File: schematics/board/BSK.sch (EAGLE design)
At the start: 56 parts

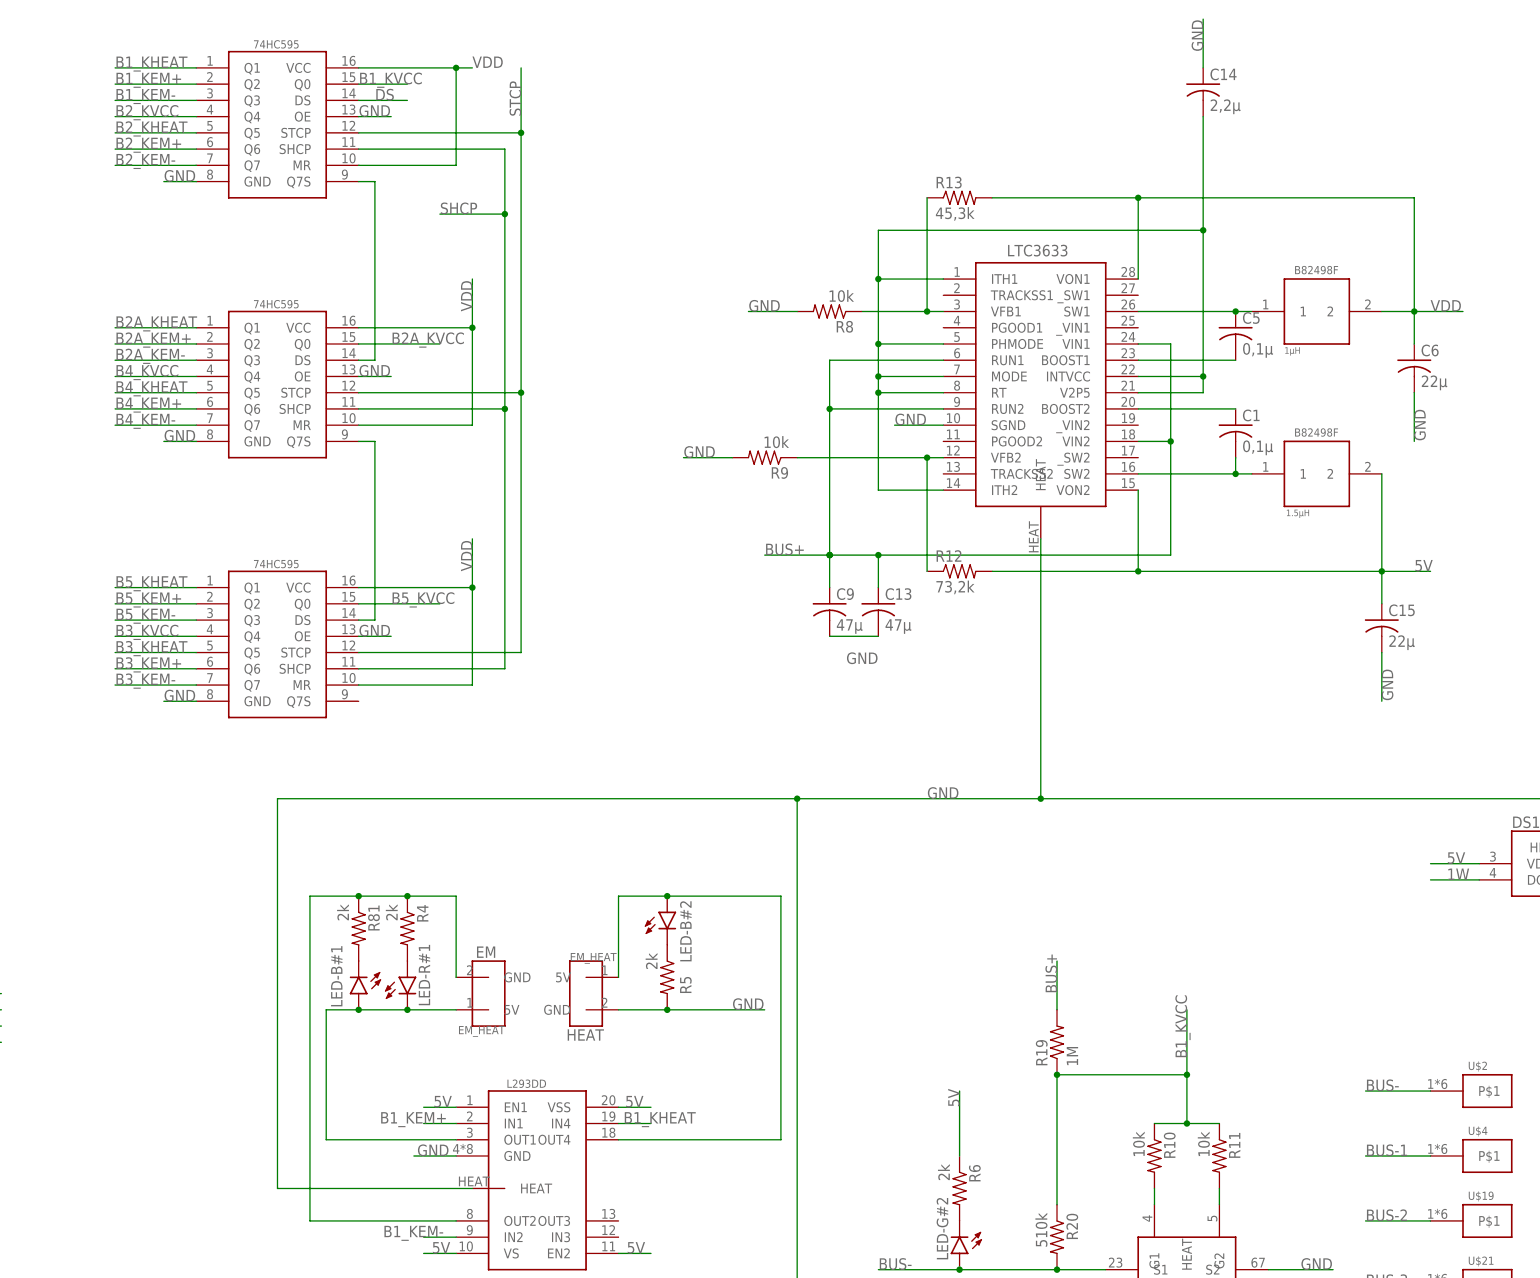
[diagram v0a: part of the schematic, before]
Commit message: Плата АРК проложена на 76%
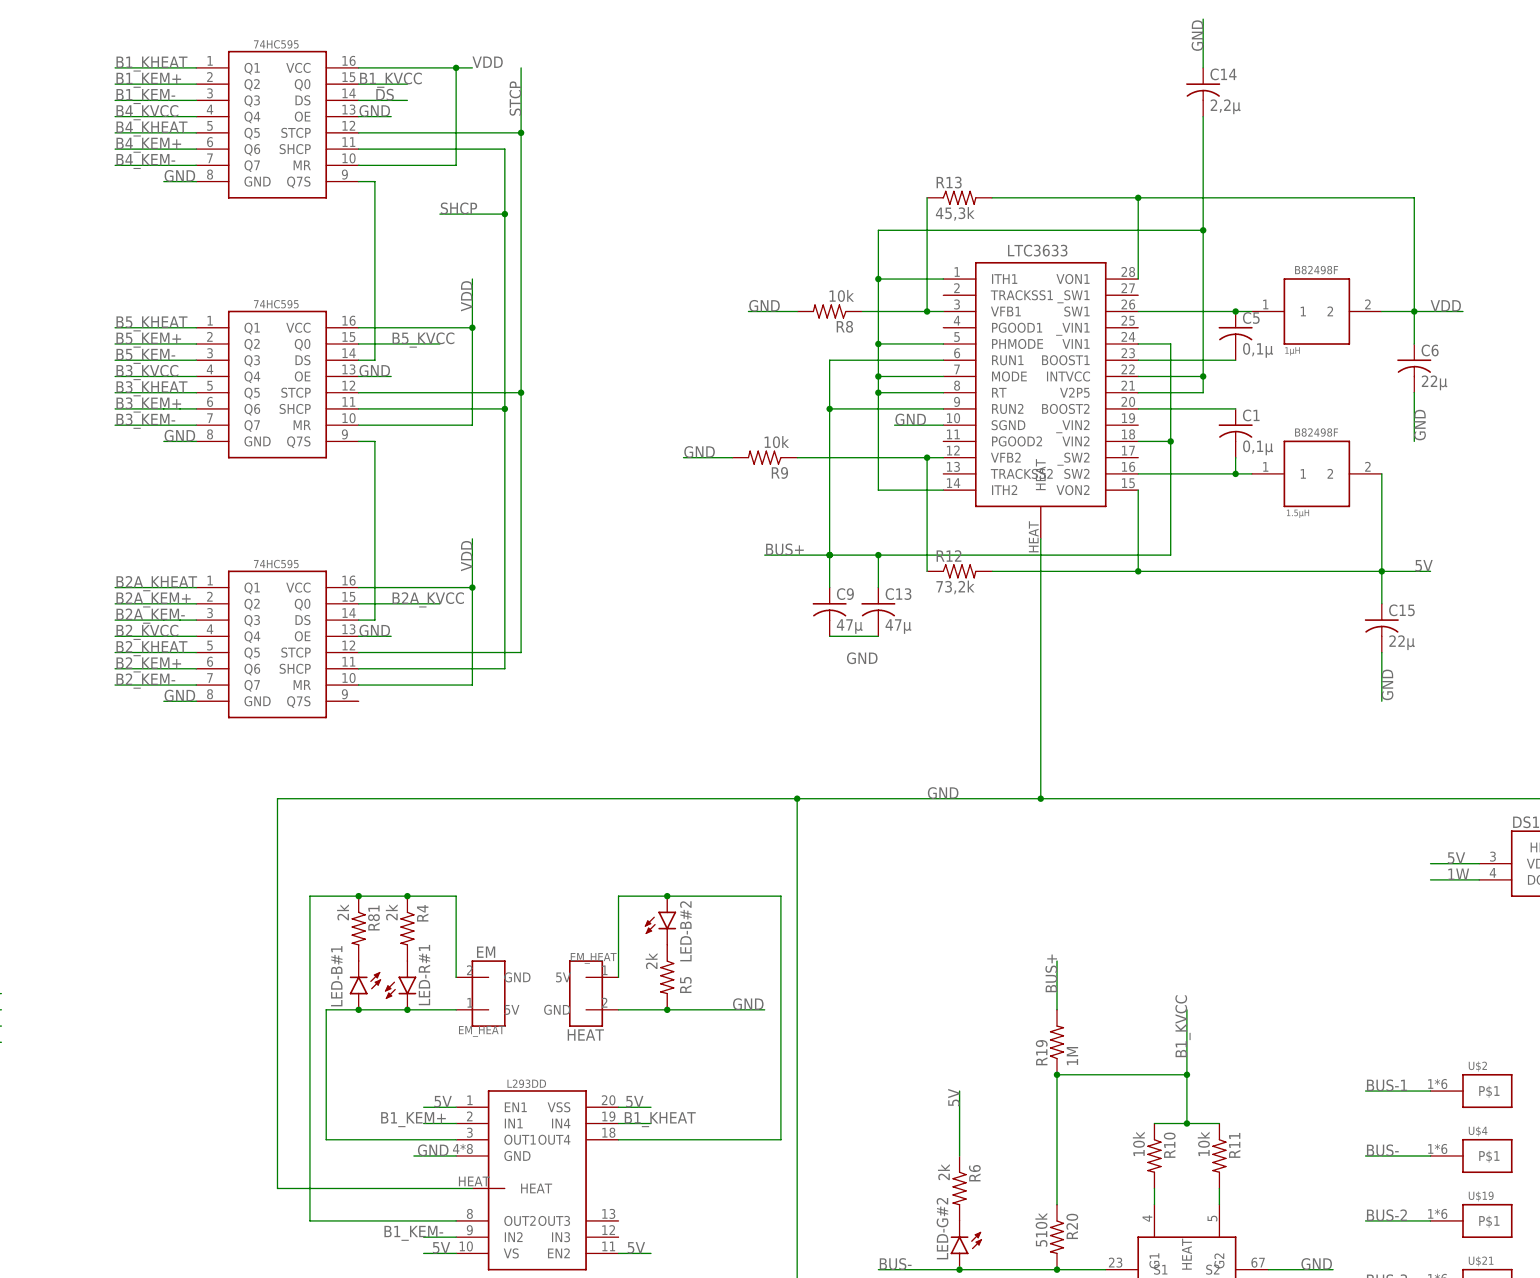
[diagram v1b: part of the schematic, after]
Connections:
- net B2A_KEM+: now also 74HC595#3.Q2; no longer 74HC595#2.Q2
- net B2A_KEM-: now also 74HC595#3.Q3; no longer 74HC595#2.Q3
- net B2A_KHEAT: now also 74HC595#3.Q1; no longer 74HC595#2.Q1
- net B2A_KVCC: now also 74HC595#3.Q0; no longer 74HC595#2.Q0
- net B2_KEM+: now also 74HC595#3.Q6; no longer 74HC595#1.Q6
- net B2_KEM-: now also 74HC595#3.Q7; no longer 74HC595#1.Q7
- net B2_KHEAT: now also 74HC595#3.Q5; no longer 74HC595#1.Q5
- net B2_KVCC: now also 74HC595#3.Q4; no longer 74HC595#1.Q4
- net B3_KEM+: now also 74HC595#2.Q6; no longer 74HC595#3.Q6
- net B3_KEM-: now also 74HC595#2.Q7; no longer 74HC595#3.Q7
- net B3_KHEAT: now also 74HC595#2.Q5; no longer 74HC595#3.Q5
- net B3_KVCC: now also 74HC595#2.Q4; no longer 74HC595#3.Q4
- net B4_KEM+: now also 74HC595#1.Q6; no longer 74HC595#2.Q6
- net B4_KEM-: now also 74HC595#1.Q7; no longer 74HC595#2.Q7
- net B4_KHEAT: now also 74HC595#1.Q5; no longer 74HC595#2.Q5
- net B4_KVCC: now also 74HC595#1.Q4; no longer 74HC595#2.Q4
- net B5_KEM+: now also 74HC595#2.Q2; no longer 74HC595#3.Q2
- net B5_KEM-: now also 74HC595#2.Q3; no longer 74HC595#3.Q3
- net B5_KHEAT: now also 74HC595#2.Q1; no longer 74HC595#3.Q1
- net B5_KVCC: now also 74HC595#2.Q0; no longer 74HC595#3.Q0
- net BUS-: now also U$4.P$1; no longer U$2.P$1
- net BUS-1: now also U$2.P$1; no longer U$4.P$1
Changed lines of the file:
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@@
 <net name="B2_KEM+" class="0">
 <segment>
-<pinref part="74HC595#1" gate="G$1" pin="Q6"/>
-<wire x1="104.14" y1="264.16" x2="91.44" y2="264.16" width="0.1524" layer="91"/>
-<label x="91.44" y="264.16" size="1.778" layer="95"/>
+<label x="91.44" y="182.88" size="1.778" layer="95"/>
+<wire x1="104.14" y1="182.88" x2="91.44" y2="182.88" width="0.1524" layer="91"/>
+<pinref part="74HC595#3" gate="G$1" pin="Q6"/>
 </segment>
 <segment>
@@
 <net name="B2_KEM-" class="0">
 <segment>
-<pinref part="74HC595#1" gate="G$1" pin="Q7"/>
-<wire x1="104.14" y1="261.62" x2="91.44" y2="261.62" width="0.1524" layer="91"/>
-<label x="91.44" y="261.62" size="1.778" layer="95"/>
+<label x="91.44" y="180.34" size="1.778" layer="95"/>
+<wire x1="104.14" y1="180.34" x2="91.44" y2="180.34" width="0.1524" layer="91"/>
+<pinref part="74HC595#3" gate="G$1" pin="Q7"/>
 </segment>
 <segment>
@@
 <net name="B2_KHEAT" class="0">
 <segment>
-<pinref part="74HC595#1" gate="G$1" pin="Q5"/>
-<wire x1="104.14" y1="266.7" x2="91.44" y2="266.7" width="0.1524" layer="91"/>
-<label x="91.44" y="266.7" size="1.778" layer="95"/>
+<label x="91.44" y="185.42" size="1.778" layer="95"/>
+<wire x1="104.14" y1="185.42" x2="91.44" y2="185.42" width="0.1524" layer="91"/>
+<pinref part="74HC595#3" gate="G$1" pin="Q5"/>
 </segment>
 <segment>
@@
 <net name="B2A_KEM+" class="0">
 <segment>
-<pinref part="74HC595#2" gate="G$1" pin="Q2"/>
-<wire x1="104.14" y1="233.68" x2="91.44" y2="233.68" width="0.1524" layer="91"/>
-<label x="91.44" y="233.68" size="1.778" layer="95"/>
+<label x="91.44" y="193.04" size="1.778" layer="95"/>
+<wire x1="104.14" y1="193.04" x2="91.44" y2="193.04" width="0.1524" layer="91"/>
+<pinref part="74HC595#3" gate="G$1" pin="Q2"/>
 </segment>
 <segment>
@@
 <net name="B2A_KEM-" class="0">
 <segment>
-<pinref part="74HC595#2" gate="G$1" pin="Q3"/>
-<wire x1="104.14" y1="231.14" x2="91.44" y2="231.14" width="0.1524" layer="91"/>
-<label x="91.44" y="231.14" size="1.778" layer="95"/>
+<label x="91.44" y="190.5" size="1.778" layer="95"/>
+<wire x1="101.6" y1="190.5" x2="99.06" y2="190.5" width="0.1524" layer="91"/>
+<pinref part="74HC595#3" gate="G$1" pin="Q3"/>
+<wire x1="99.06" y1="190.5" x2="91.44" y2="190.5" width="0.1524" layer="91"/>
+<wire x1="101.6" y1="190.5" x2="104.14" y2="190.5" width="0.1524" layer="91"/>
 </segment>
 <segment>
@@
 <net name="B2A_KHEAT" class="0">
 <segment>
-<pinref part="74HC595#2" gate="G$1" pin="Q1"/>
-<wire x1="104.14" y1="236.22" x2="91.44" y2="236.22" width="0.1524" layer="91"/>
-<label x="91.44" y="236.22" size="1.778" layer="95"/>
+<label x="91.44" y="195.58" size="1.778" layer="95"/>
+<wire x1="104.14" y1="195.58" x2="91.44" y2="195.58" width="0.1524" layer="91"/>
+<pinref part="74HC595#3" gate="G$1" pin="Q1"/>
 </segment>
 <segment>
@@
 </segment>
 <segment>
-<pinref part="74HC595#3" gate="G$1" pin="Q6"/>
-<wire x1="104.14" y1="182.88" x2="91.44" y2="182.88" width="0.1524" layer="91"/>
-<label x="91.44" y="182.88" size="1.778" layer="95"/>
+<label x="91.44" y="223.52" size="1.778" layer="95"/>
+<wire x1="101.6" y1="223.52" x2="99.06" y2="223.52" width="0.1524" layer="91"/>
+<pinref part="74HC595#2" gate="G$1" pin="Q6"/>
+<wire x1="99.06" y1="223.52" x2="91.44" y2="223.52" width="0.1524" layer="91"/>
+<wire x1="104.14" y1="223.52" x2="101.6" y2="223.52" width="0.1524" layer="91"/>
 </segment>
 </net>
@@
 </segment>
 <segment>
-<pinref part="74HC595#3" gate="G$1" pin="Q7"/>
-<wire x1="104.14" y1="180.34" x2="91.44" y2="180.34" width="0.1524" layer="91"/>
-<label x="91.44" y="180.34" size="1.778" layer="95"/>
+<label x="91.44" y="220.98" size="1.778" layer="95"/>
+<wire x1="104.14" y1="220.98" x2="91.44" y2="220.98" width="0.1524" layer="91"/>
+<pinref part="74HC595#2" gate="G$1" pin="Q7"/>
 </segment>
 </net>
@@
 </segment>
 <segment>
-<pinref part="74HC595#3" gate="G$1" pin="Q5"/>
-<wire x1="104.14" y1="185.42" x2="91.44" y2="185.42" width="0.1524" layer="91"/>
-<label x="91.44" y="185.42" size="1.778" layer="95"/>
+<label x="91.44" y="226.06" size="1.778" layer="95"/>
+<wire x1="104.14" y1="226.06" x2="91.44" y2="226.06" width="0.1524" layer="91"/>
+<pinref part="74HC595#2" gate="G$1" pin="Q5"/>
 </segment>
 </net>
@@
 </segment>
 <segment>
-<pinref part="74HC595#2" gate="G$1" pin="Q5"/>
-<wire x1="104.14" y1="226.06" x2="91.44" y2="226.06" width="0.1524" layer="91"/>
-<label x="91.44" y="226.06" size="1.778" layer="95"/>
+<label x="91.44" y="266.7" size="1.778" layer="95"/>
+<wire x1="104.14" y1="266.7" x2="91.44" y2="266.7" width="0.1524" layer="91"/>
+<pinref part="74HC595#1" gate="G$1" pin="Q5"/>
 </segment>
 </net>
 <net name="B5_KEM+" class="0">
 <segment>
-<pinref part="74HC595#3" gate="G$1" pin="Q2"/>
-<wire x1="104.14" y1="193.04" x2="91.44" y2="193.04" width="0.1524" layer="91"/>
-<label x="91.44" y="193.04" size="1.778" layer="95"/>
+<label x="91.44" y="233.68" size="1.778" layer="95"/>
+<wire x1="104.14" y1="233.68" x2="91.44" y2="233.68" width="0.1524" layer="91"/>
+<pinref part="74HC595#2" gate="G$1" pin="Q2"/>
 </segment>
 <segment>
@@
 <net name="B5_KEM-" class="0">
 <segment>
-<pinref part="74HC595#3" gate="G$1" pin="Q3"/>
-<wire x1="104.14" y1="190.5" x2="91.44" y2="190.5" width="0.1524" layer="91"/>
-<label x="91.44" y="190.5" size="1.778" layer="95"/>
+<label x="91.44" y="231.14" size="1.778" layer="95"/>
+<wire x1="104.14" y1="231.14" x2="91.44" y2="231.14" width="0.1524" layer="91"/>
+<pinref part="74HC595#2" gate="G$1" pin="Q3"/>
 </segment>
 <segment>
@@
 <net name="B5_KHEAT" class="0">
 <segment>
-<pinref part="74HC595#3" gate="G$1" pin="Q1"/>
-<wire x1="104.14" y1="195.58" x2="91.44" y2="195.58" width="0.1524" layer="91"/>
-<label x="91.44" y="195.58" size="1.778" layer="95"/>
+<label x="91.44" y="236.22" size="1.778" layer="95"/>
+<wire x1="104.14" y1="236.22" x2="91.44" y2="236.22" width="0.1524" layer="91"/>
+<pinref part="74HC595#2" gate="G$1" pin="Q1"/>
 </segment>
 <segment>
@@
 <net name="B2_KVCC" class="0">
 <segment>
-<pinref part="74HC595#1" gate="G$1" pin="Q4"/>
-<wire x1="104.14" y1="269.24" x2="91.44" y2="269.24" width="0.1524" layer="91"/>
-<label x="91.44" y="269.24" size="1.778" layer="95"/>
+<label x="91.44" y="187.96" size="1.778" layer="95"/>
+<wire x1="104.14" y1="187.96" x2="91.44" y2="187.96" width="0.1524" layer="91"/>
+<pinref part="74HC595#3" gate="G$1" pin="Q4"/>
 </segment>
 <segment>
@@
 <net name="B2A_KVCC" class="0">
 <segment>
-<pinref part="74HC595#2" gate="G$1" pin="Q0"/>
-<wire x1="129.54" y1="233.68" x2="142.24" y2="233.68" width="0.1524" layer="91"/>
-<label x="134.62" y="233.68" size="1.778" layer="95"/>
+<label x="134.62" y="193.04" size="1.778" layer="95"/>
+<wire x1="129.54" y1="193.04" x2="142.24" y2="193.04" width="0.1524" layer="91"/>
+<pinref part="74HC595#3" gate="G$1" pin="Q0"/>
 </segment>
 <segment>
@@
 </segment>
 <segment>
-<pinref part="74HC595#3" gate="G$1" pin="Q4"/>
-<wire x1="104.14" y1="187.96" x2="91.44" y2="187.96" width="0.1524" layer="91"/>
-<label x="91.44" y="187.96" size="1.778" layer="95"/>
+<label x="91.44" y="228.6" size="1.778" layer="95"/>
+<wire x1="104.14" y1="228.6" x2="91.44" y2="228.6" width="0.1524" layer="91"/>
+<pinref part="74HC595#2" gate="G$1" pin="Q4"/>
 </segment>
 </net>
 <net name="B5_KVCC" class="0">
 <segment>
-<pinref part="74HC595#3" gate="G$1" pin="Q0"/>
-<wire x1="129.54" y1="193.04" x2="142.24" y2="193.04" width="0.1524" layer="91"/>
-<label x="134.62" y="193.04" size="1.778" layer="95"/>
+<label x="134.62" y="233.68" size="1.778" layer="95"/>
+<wire x1="129.54" y1="233.68" x2="142.24" y2="233.68" width="0.1524" layer="91"/>
+<pinref part="74HC595#2" gate="G$1" pin="Q0"/>
 </segment>
 <segment>
@@
 </segment>
 <segment>
-<pinref part="74HC595#2" gate="G$1" pin="Q4"/>
-<wire x1="104.14" y1="228.6" x2="91.44" y2="228.6" width="0.1524" layer="91"/>
-<label x="91.44" y="228.6" size="1.778" layer="95"/>
+<label x="91.44" y="269.24" size="1.778" layer="95"/>
+<wire x1="104.14" y1="269.24" x2="91.44" y2="269.24" width="0.1524" layer="91"/>
+<pinref part="74HC595#1" gate="G$1" pin="Q4"/>
 </segment>
 </net>
@@
 </segment>
 <segment>
-<pinref part="U$2" gate="G$1" pin="P$1"/>
-<wire x1="297.18" y1="116.84" x2="287.02" y2="116.84" width="0.1524" layer="91"/>
-<label x="287.02" y="116.84" size="1.778" layer="95"/>
+<label x="287.02" y="106.68" size="1.778" layer="95"/>
+<wire x1="297.18" y1="106.68" x2="287.02" y2="106.68" width="0.1524" layer="91"/>
+<pinref part="U$4" gate="G$1" pin="P$1"/>
 </segment>
 </net>
@@
 </segment>
 <segment>
-<pinref part="74HC595#2" gate="G$1" pin="Q6"/>
-<wire x1="104.14" y1="223.52" x2="91.44" y2="223.52" width="0.1524" layer="91"/>
-<label x="91.44" y="223.52" size="1.778" layer="95"/>
+<label x="91.44" y="264.16" size="1.778" layer="95"/>
+<wire x1="104.14" y1="264.16" x2="91.44" y2="264.16" width="0.1524" layer="91"/>
+<pinref part="74HC595#1" gate="G$1" pin="Q6"/>
 </segment>
 </net>
@@
 </segment>
 <segment>
-<pinref part="74HC595#2" gate="G$1" pin="Q7"/>
-<wire x1="104.14" y1="220.98" x2="91.44" y2="220.98" width="0.1524" layer="91"/>
-<label x="91.44" y="220.98" size="1.778" layer="95"/>
+<label x="91.44" y="261.62" size="1.778" layer="95"/>
+<wire x1="104.14" y1="261.62" x2="91.44" y2="261.62" width="0.1524" layer="91"/>
+<pinref part="74HC595#1" gate="G$1" pin="Q7"/>
 </segment>
 </net>
@@
 <net name="BUS-1" class="0">
 <segment>
-<pinref part="U$4" gate="G$1" pin="P$1"/>
-<wire x1="297.18" y1="106.68" x2="287.02" y2="106.68" width="0.1524" layer="91"/>
-<label x="287.02" y="106.68" size="1.778" layer="95"/>
-</segment>
-</net>
+<label x="287.02" y="116.84" size="1.778" layer="95"/>
+<wire x1="297.18" y1="116.84" x2="287.02" y2="116.84" width="0.1524" layer="91"/>
+<pinref part="U$2" gate="G$1" pin="P$1"/>
+</segment>
+</net>
